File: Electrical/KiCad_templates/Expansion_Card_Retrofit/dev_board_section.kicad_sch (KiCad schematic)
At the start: 25 parts, among them Q1 DMG1012T, Q2 Q_PMOS_SGD, Q3 Q_NMOS_DGS, SW2 SW_Push, U2 RP2040, U3 W25Q16JVUXIQ

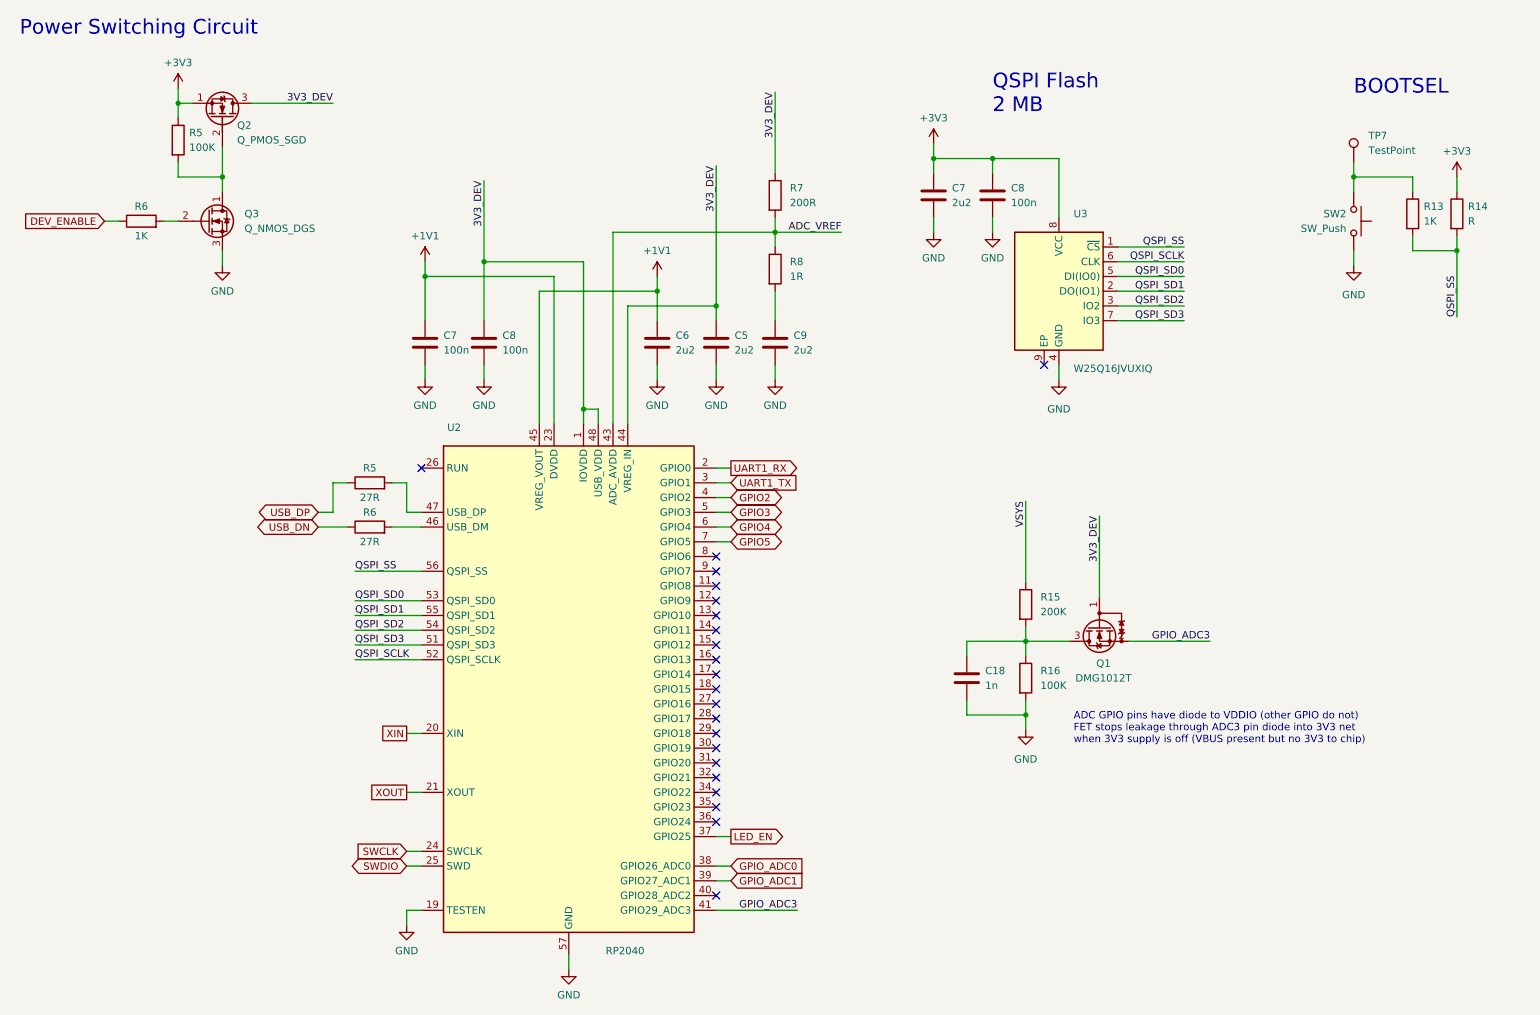
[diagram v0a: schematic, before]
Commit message: Main layout of chip sections finished
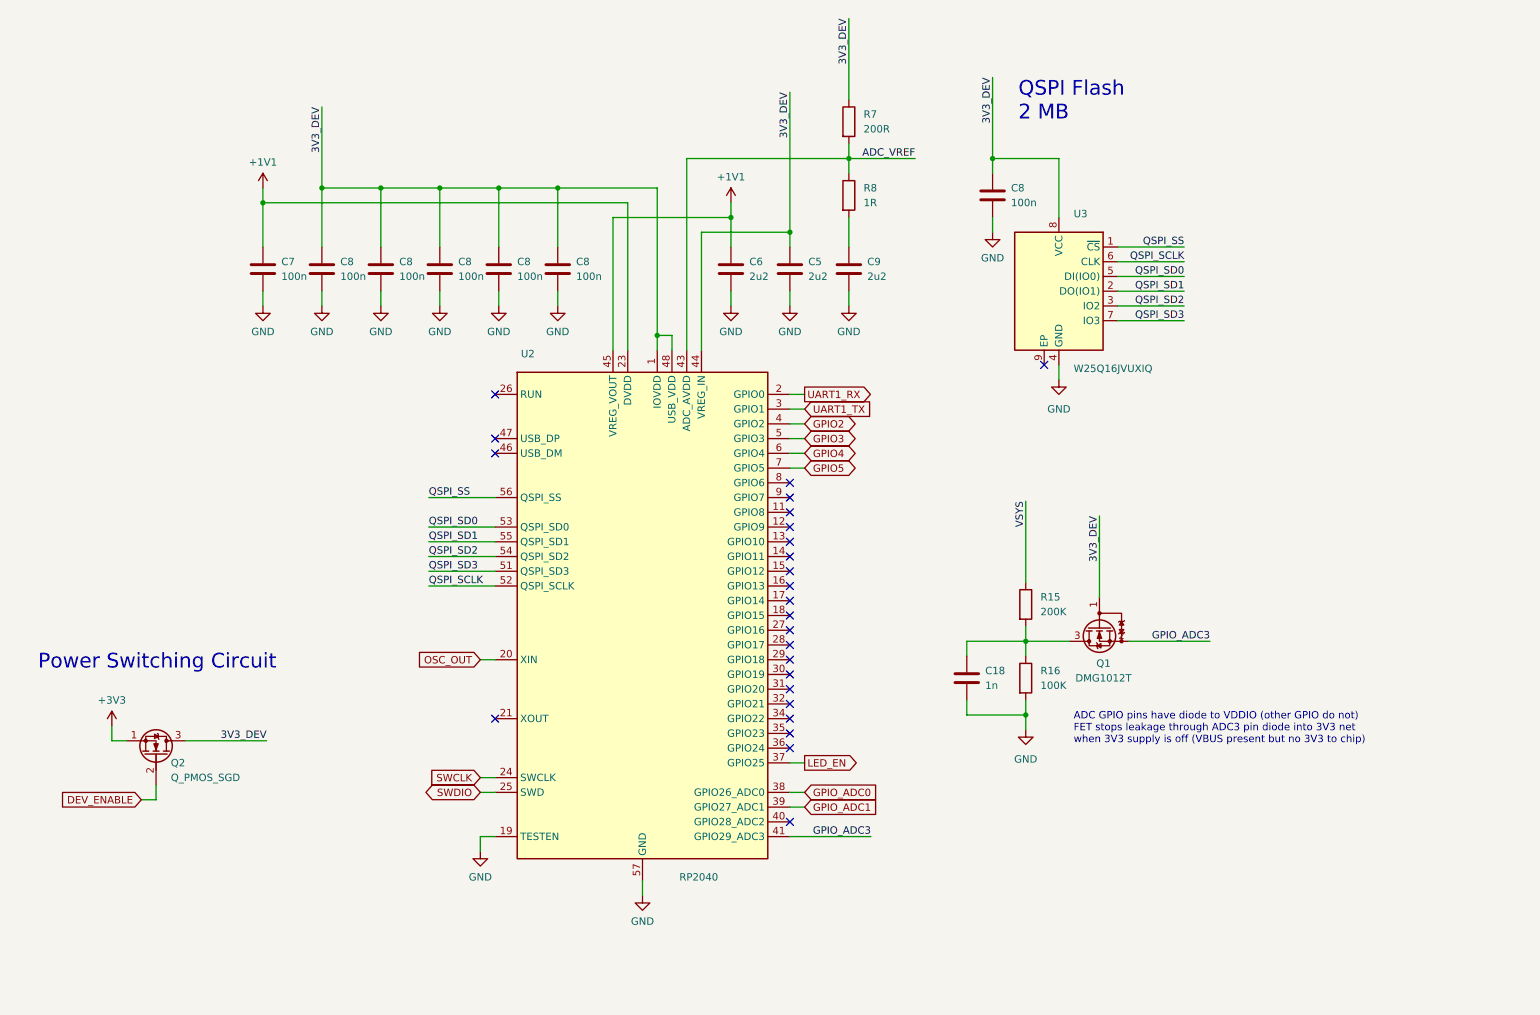
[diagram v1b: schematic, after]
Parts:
- removed C7: 2u2, Capacitor_SMD:C_0402_1005Metric, symbol Device:C
- removed Q3: Q_NMOS_DGS, Package_TO_SOT_SMD:SOT-523, symbol Device:Q_NMOS_DGS
- removed R13, R6: 1K, Resistor_SMD:R_0402_1005Metric, symbol Device:R
- removed R14: R, Resistor_SMD:R_0402_1005Metric, symbol Device:R
- removed R5: 100K, Resistor_SMD:R_0402_1005Metric, symbol Device:R
- removed R5, R6: 27R, Resistor_SMD:R_0201_0603Metric, symbol Device:R
- removed SW2: SW_Push, symbol Switch:SW_Push
- removed TP7: TestPoint, TestPoint:TestPoint_Pad_1.5x1.5mm, symbol Connector:TestPoint
- added C8 (x4): 100n, Capacitor_SMD:C_0201_0603Metric, symbol Device:C
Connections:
- net +3V3: no longer C8.1, U3.8 (VCC)
- net 3V3_DEV: now also C8.1, U3.8 (VCC), C8.1, C8.1, C8.1, C8.1
- net DEV_ENABLE: now also Q2.2 (G)
- net GND: now also C8.2, C8.2, C8.2, C8.2
- net XIN renamed OSC_OUT
- net XOUT: no longer names the net of U2.21 (XOUT)
- no-connect marks 22 -> 25
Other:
- note removed: "BOOTSEL"
- moved on the sheet: C5, C6, C7, C8, C9, Q2, R7, R8, U2

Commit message: Current state before flash footprint update
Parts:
- removed U3: W25Q16JVUXIQ, Package_SON:WSON-8-1EP_6x5mm_P1.27mm_EP3.4x4.3mm, symbol Memory_Flash:W25Q32JVZP
- added U3: W25Q16JVUXIQ, SnapEDA:IC_W25Q16JVUXIQ_TR, symbol SnapEDA:W25Q16JVUXIQ_TR
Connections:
- net 3V3_DEV: now also U3.8 (VCC)
- net GND: now also U3.4 (GND)
- net QSPI_SCLK: now also U3.6 (CLK)
- net QSPI_SD0: now also U3.5 (DI/IO0)
- net QSPI_SD1: now also U3.2 (DO/IO1)
- net QSPI_SD2: now also U3.3 (~{WP}/IO2)
- net QSPI_SD3: now also U3.7 (~{HOLD}/~{RESET}/IO3)
- net QSPI_SS: now also U3.1 (~{CS})
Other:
- moved on the sheet: C18, C8, Q1, R15, R16

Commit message: First complete version
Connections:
- net VSYS renamed VBUS
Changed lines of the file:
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@@
-    (stroke (width 0) (type default))
-  )
-  (wire (pts (xy 201.93 103.505) (xy 201.93 117.475))
     (stroke (width 0) (type default))
   )
@@
   )
   (wire (pts (xy 125.73 168.275) (xy 125.73 170.815))
+    (stroke (width 0) (type default))
+  )
+  (wire (pts (xy 201.93 114.935) (xy 201.93 117.475))
     (stroke (width 0) (type default))
   )
@@
   )
   (label "GPIO_ADC3" (at 233.68 127.635 180) (fields_autoplaced)
-    (effects (font (size 1.27 1.27)) (justify right bottom))
-  )
-  (label "VSYS" (at 201.93 103.505 270) (fields_autoplaced)
     (effects (font (size 1.27 1.27)) (justify right bottom))
   )
@@
         )
       )
+    )
+  )
+  (symbol (lib_id "power:VBUS") (at 201.93 114.935 0) (unit 1)
+    (in_bom yes) (on_board yes) (dnp no) (fields_autoplaced)
+    (property "Reference" "#PWR08" (at 201.93 118.745 0)
+      (effects (font (size 1.27 1.27)) hide)
+    )
+    (property "Value" "VBUS" (at 201.93 110.49 0)
+      (effects (font (size 1.27 1.27)))
+    )
+    (property "Footprint" "" (at 201.93 114.935 0)
+      (effects (font (size 1.27 1.27)) hide)
+    )
+    (property "Datasheet" "" (at 201.93 114.935 0)
+      (effects (font (size 1.27 1.27)) hide)
+    )
+    (pin "1")
+    (instances
+      (project "Expansion_Card_Retrofit"
+        (path "/fd9cf59f-f670-406e-98d4-36112036cae5/ba09e9cc-93bf-4b37-819d-b7ee30f73540"
+          (reference "#PWR08") (unit 1)
+        )
+      )

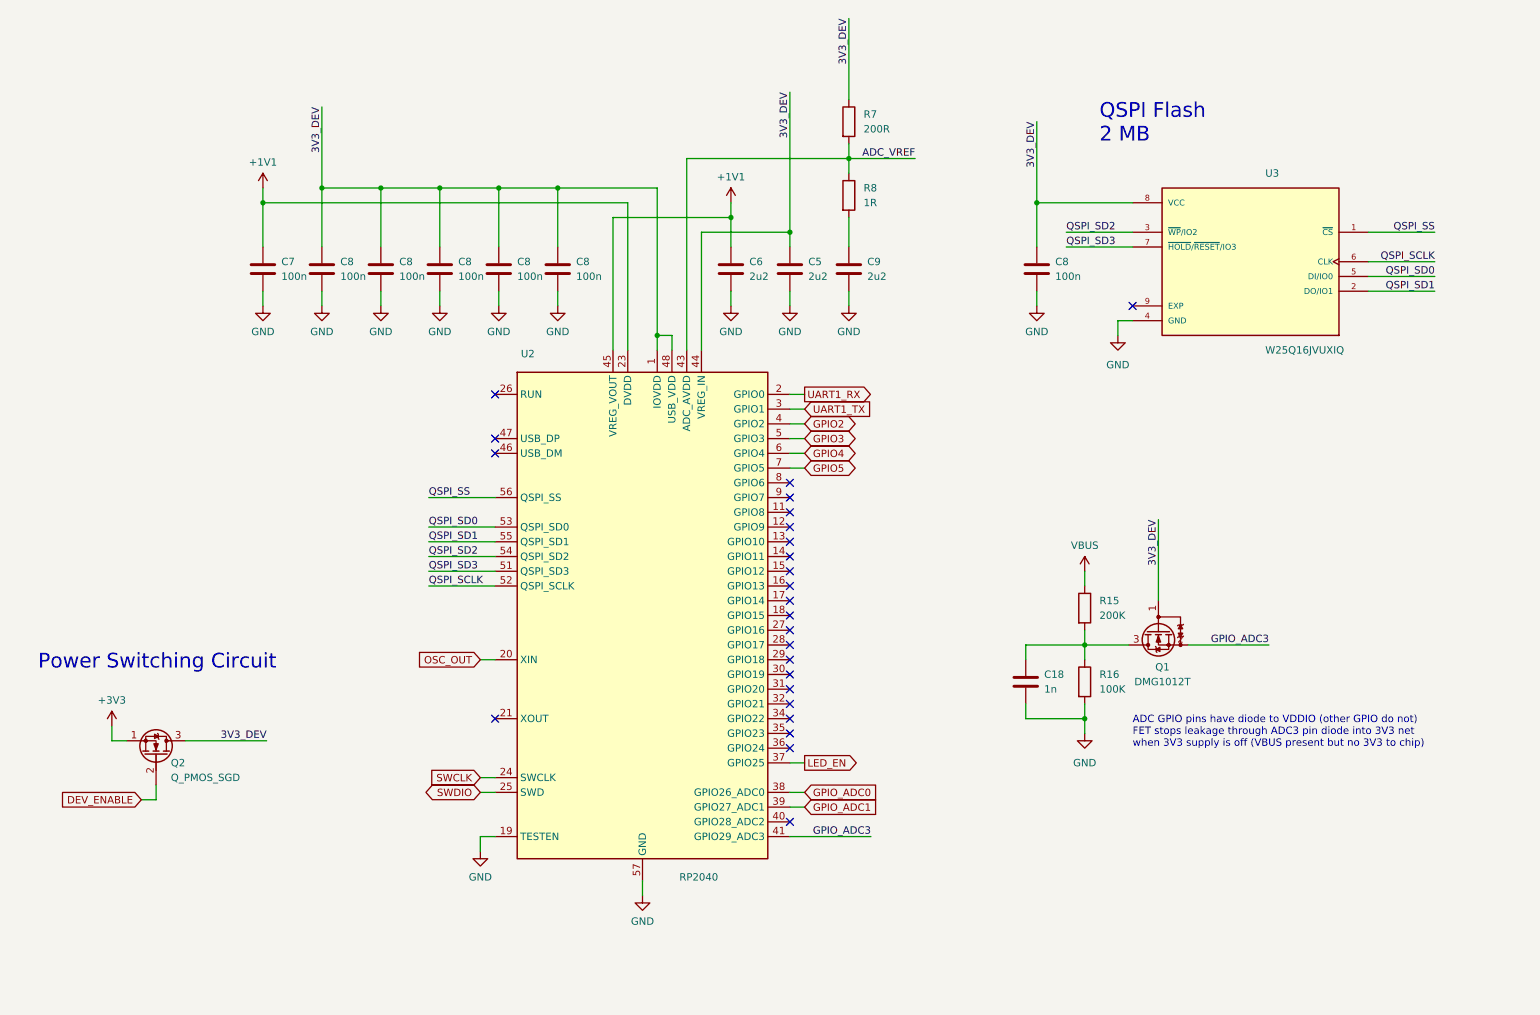
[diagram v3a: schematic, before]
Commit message: All footprints placed single-sided
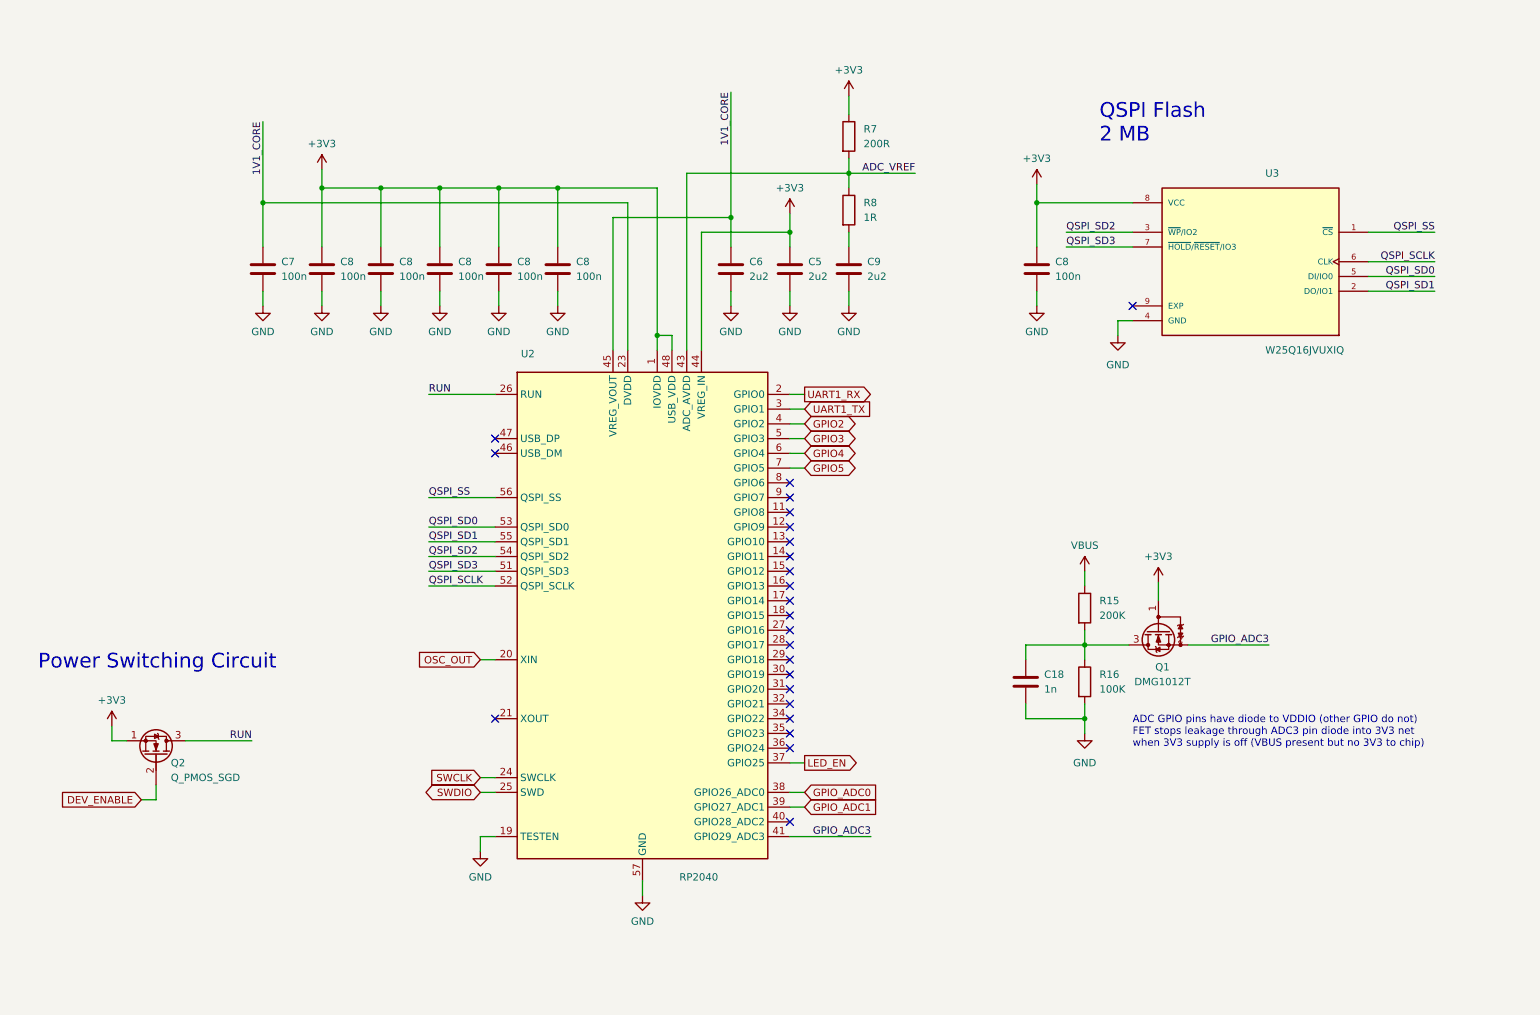
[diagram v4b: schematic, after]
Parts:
- Q1, Q2: footprint Package_TO_SOT_SMD:SOT-523 -> Package_DFN_QFN:Diodes_DFN1006-3
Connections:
- net +3V3: now also C5.1, C8.1, C8.1, C8.1, C8.1, C8.1, C8.1, Q1.1 (G), R7.1, U2.1 (IOVDD), U2.10 (IOVDD), U2.22 (IOVDD), U2.33 (IOVDD), U2.42 (IOVDD), U2.44 (VREG_IN), U2.48 (USB_VDD), U2.49 (IOVDD), U3.8 (VCC)
- net RUN: now reaches U2.26 (RUN)
- net RUN: now also Q2.3 (D)
- net +1V1 renamed 1V1_CORE
- removed net 3V3_DEV: C5.1, C8.1, C8.1, C8.1, C8.1, C8.1, C8.1, Q1.1 (G), Q2.3 (D), R7.1, U2.1 (IOVDD), U2.10 (IOVDD), U2.22 (IOVDD), U2.33 (IOVDD), U2.42 (IOVDD), U2.44 (VREG_IN), U2.48 (USB_VDD), U2.49 (IOVDD), U3.8 (VCC)
- no-connect marks 25 -> 24
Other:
- moved on the sheet: R7, R8

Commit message: Resized components to 0402 minimum
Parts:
- C18, C7, C8: footprint Capacitor_SMD:C_0201_0603Metric -> Capacitor_SMD:C_0402_1005Metric
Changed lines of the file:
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@@
       (effects (font (size 1.27 1.27)) (justify left))
     )
-    (property "Footprint" "Capacitor_SMD:C_0201_0603Metric" (at 91.7702 66.675 0)
+    (property "Footprint" "Capacitor_SMD:C_0402_1005Metric" (at 91.7702 66.675 0)
       (effects (font (size 1.27 1.27)) hide)
     )
@@
       (effects (font (size 1.27 1.27)) (justify left))
     )
-    (property "Footprint" "Capacitor_SMD:C_0201_0603Metric" (at 194.6402 66.675 0)
+    (property "Footprint" "Capacitor_SMD:C_0402_1005Metric" (at 194.6402 66.675 0)
       (effects (font (size 1.27 1.27)) hide)
     )
@@
       (effects (font (size 1.27 1.27)) (justify left))
     )
-    (property "Footprint" "Capacitor_SMD:C_0201_0603Metric" (at 192.7352 137.795 0)
+    (property "Footprint" "Capacitor_SMD:C_0402_1005Metric" (at 192.7352 137.795 0)
       (effects (font (size 1.27 1.27)) hide)
     )
@@
       (effects (font (size 1.27 1.27)) (justify left))
     )
-    (property "Footprint" "Capacitor_SMD:C_0201_0603Metric" (at 101.9302 66.675 0)
+    (property "Footprint" "Capacitor_SMD:C_0402_1005Metric" (at 101.9302 66.675 0)
       (effects (font (size 1.27 1.27)) hide)
     )
@@
       (effects (font (size 1.27 1.27)) (justify left))
     )
-    (property "Footprint" "Capacitor_SMD:C_0201_0603Metric" (at 71.4502 66.675 0)
+    (property "Footprint" "Capacitor_SMD:C_0402_1005Metric" (at 71.4502 66.675 0)
       (effects (font (size 1.27 1.27)) hide)
     )
@@
       (effects (font (size 1.27 1.27)) (justify left))
     )
-    (property "Footprint" "Capacitor_SMD:C_0201_0603Metric" (at 112.0902 66.675 0)
+    (property "Footprint" "Capacitor_SMD:C_0402_1005Metric" (at 112.0902 66.675 0)
       (effects (font (size 1.27 1.27)) hide)
     )
@@
       (effects (font (size 1.27 1.27)) (justify left))
     )
-    (property "Footprint" "Capacitor_SMD:C_0201_0603Metric" (at 81.6102 66.675 0)
+    (property "Footprint" "Capacitor_SMD:C_0402_1005Metric" (at 81.6102 66.675 0)
       (effects (font (size 1.27 1.27)) hide)
     )
@@
       (effects (font (size 1.27 1.27)) (justify left))
     )
-    (property "Footprint" "Capacitor_SMD:C_0201_0603Metric" (at 61.2902 66.675 0)
-      (effects (font (size 1.27 1.27)) hide)
-    )
+    (property "Footprint" "Capacitor_SMD:C_0402_1005Metric" (at 61.2902 66.675 0)
+      (effects (font (size 1.27 1.27)) hide)
+    )
